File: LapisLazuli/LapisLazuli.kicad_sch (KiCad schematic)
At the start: 50 parts, among them J1 Screw_Terminal_01x01, J10 Conn_01x02, J11 Conn_01x02, J12 Conn_01x02, J13 Screw_Terminal_01x01, J14 Conn_01x02, J2 Screw_Terminal_01x01, J3 Conn_01x02, J4 Conn_01x02, J5 Conn_01x02, J6 Conn_01x02, J7 Conn_01x02, J8 Conn_01x02, J9 Conn_01x02, Q1 IRLU024NPBF, Q2 IRLU024NPBF, Q3 IRLU024NPBF, Q4 IRLU024NPBF, U1 TSR_1-2412, U2 DRV8231ADSG, U3 DRV8231ADSG, U4 DRV8231ADSG, U5 SN65HVD485EDR

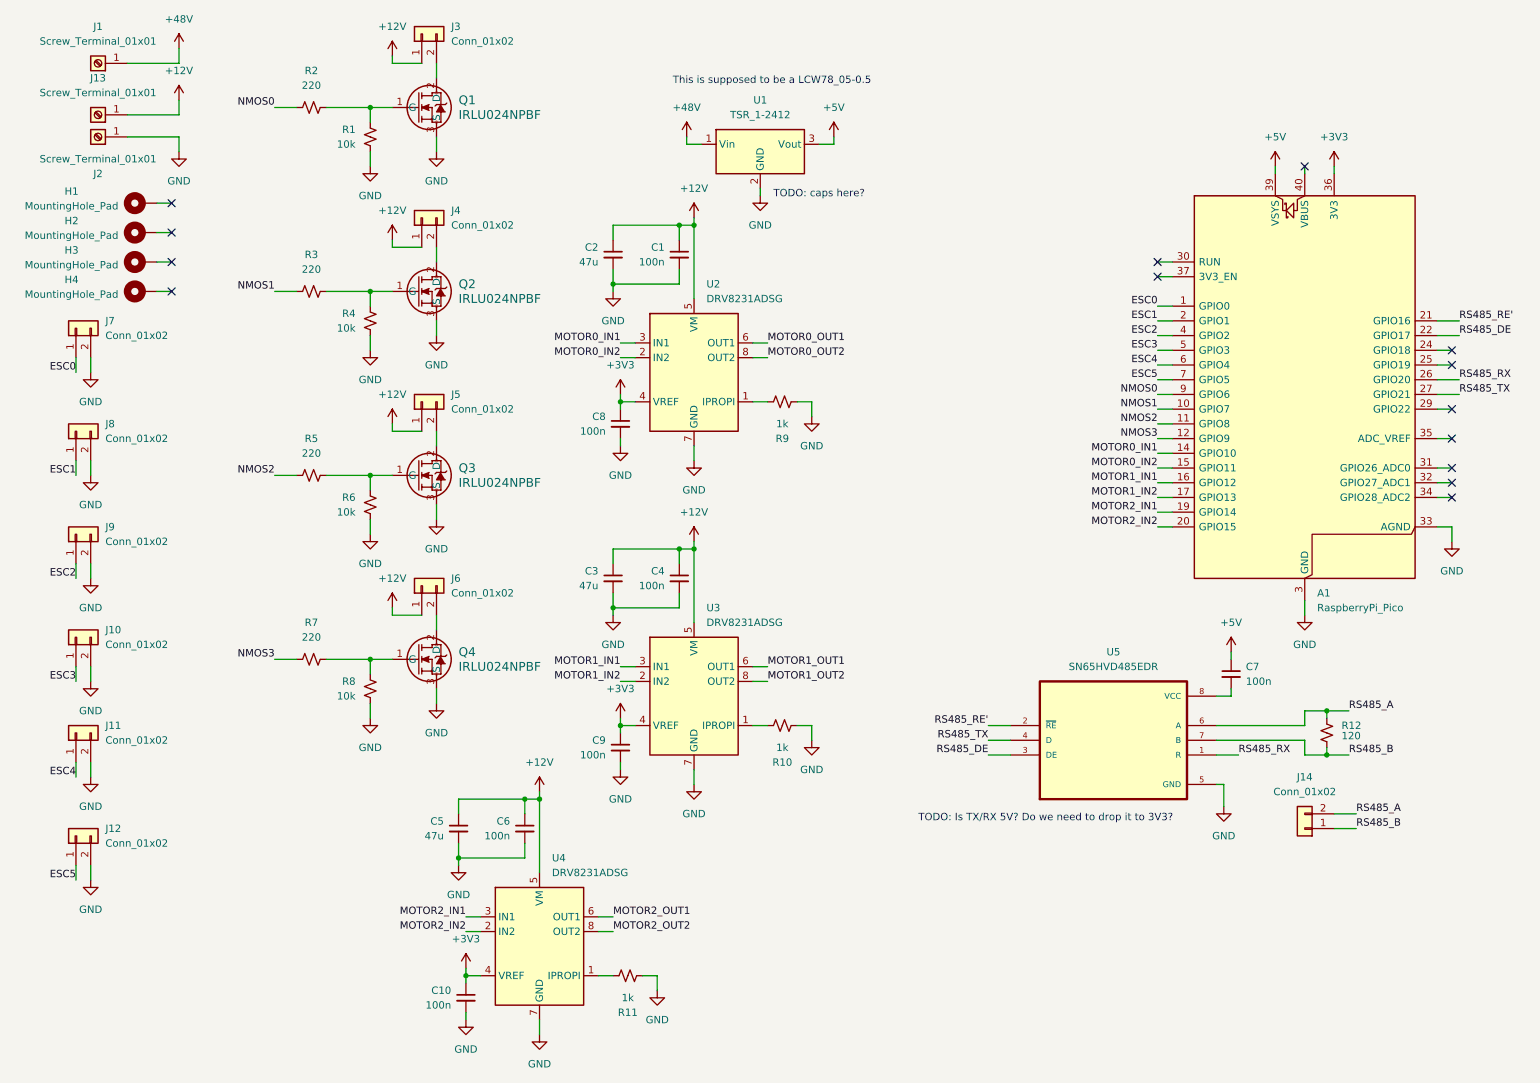
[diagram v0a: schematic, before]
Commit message: update lapis schematic
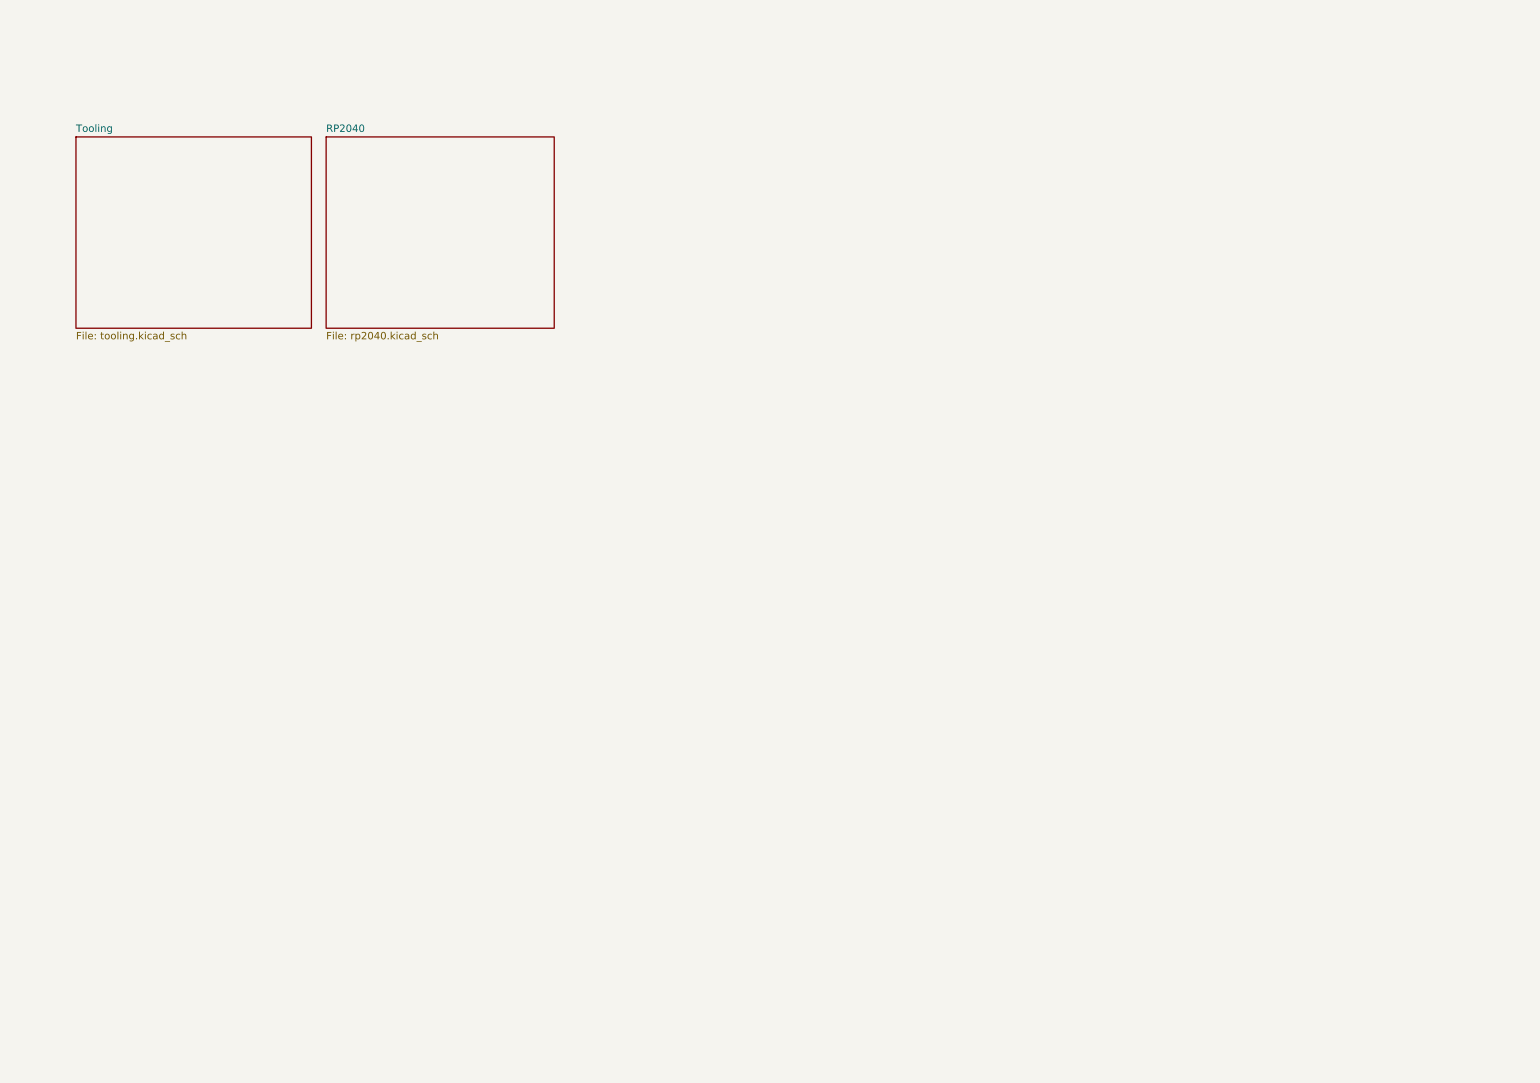
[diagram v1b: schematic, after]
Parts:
- removed A1: RaspberryPi_Pico, Module:RaspberryPi_Pico_Common_Unspecified, symbol MCU_Module:RaspberryPi_Pico
- removed C1, C10, C4, C6, C7, C8, C9: 100n, symbol Device:C_Small
- removed C2, C3, C5: 47u, symbol Device:C_Small
- removed H1, H2, H3, H4: MountingHole_Pad, symbol Mechanical:MountingHole_Pad
- removed J1, J13, J2: Screw_Terminal_01x01, symbol Connector:Screw_Terminal_01x01
- removed J10, J11, J12, J14, J3, J4, J5, J6, J7, J8, J9: Conn_01x02, symbol Connector_Generic:Conn_01x02
- removed Q1, Q2, Q3, Q4: IRLU024NPBF, PG-TO251-3-901_INF, symbol 2025-10-07_14-28-17:IRLU024NPBF
- removed R1, R4, R6, R8: 10k, symbol Device:R_Small_US
- removed R10, R11, R9: 1k, symbol Device:R_Small_US
- removed R12: 120, symbol Device:R_Small_US
- removed R2, R3, R5, R7: 220, symbol Device:R_Small_US
- removed U1: TSR_1-2412, Converter_DCDC:Converter_DCDC_TRACO_TSR-1_THT, symbol Regulator_Switching:TSR_1-2412
- removed U2, U3, U4: DRV8231ADSG, Package_SON:WSON-8-1EP_2x2mm_P0.5mm_EP0.9x1.6mm, symbol Driver_Motor:DRV8231ADSG
- removed U5: SN65HVD485EDR, footprints:SOIC127P599X175-8N, symbol SN65HVD485EDR:SN65HVD485EDR
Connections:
- no-connect marks 14 -> 0
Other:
- added sheet RP2040 (rp2040.kicad_sch)
- added sheet Tooling (tooling.kicad_sch)
- note removed: "TODO: Is TX/RX 5V? Do we need to drop it to 3V3?"
- note removed: "TODO: caps here?"
- note removed: "This is supposed to be a LCW78_05-0.5"

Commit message: Zaid Schematic Review
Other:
- sheet RP2040 ports: added ESC0, ESC1, ESC2, ESC3, ESC4, ESC5, I2C_MUX_RESET', I2C_SCL, I2C_SDA, LED0, LED1, MOTOR0_DIR, MOTOR0_PWM, MOTOR1_DIR, MOTOR1_PWM, MOTOR2_DIR, MOTOR2_PWM, MOTOR3_DIR, MOTOR3_PWM, RS485_RX, RS485_SEND, RS485_TX, SERVO0, SERVO1, SERVO2, SERVO3; removed none
- sheet Tooling ports: added ESC0, ESC1, ESC2, ESC3, ESC4, ESC5, I2C_MUX_RESET', I2C_SCL, I2C_SDA, LED0, LED1, MOTOR0_DIR, MOTOR0_PWM, MOTOR1_DIR, MOTOR1_PWM, MOTOR2_DIR, MOTOR2_PWM, MOTOR3_DIR, MOTOR3_PWM, RS485_RX, RS485_SEND, RS485_TX, SERVO0, SERVO1, SERVO2, SERVO3; removed none
